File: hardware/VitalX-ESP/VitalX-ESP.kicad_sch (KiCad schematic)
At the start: 45 parts, among them J1 ECG Probe, J2 GSR Probe, Q1 BSS138, U1 AD8232ACPZ-R7, U2 ESP32-WROOM-32U, U3 ADP160AUJZ-1.8-R7, U4 ADPD144RI-ACEZ-RL, U5 AMS1117-3.3, U6 MCP601-xOT

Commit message: [nightly] Initial esp32-s2-wroom configuration.
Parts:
- removed U2: ESP32-WROOM-32U, RF_Module:ESP32-WROOM-32U, symbol RF_Module:ESP32-WROOM-32U
- added C14: 22u, Capacitor_SMD:C_0603_1608Metric, symbol Device:C_Small
- added C15: 100n, Capacitor_SMD:C_0603_1608Metric, symbol Device:C_Small
- added C16: 1u, Capacitor_SMD:C_0603_1608Metric, symbol Device:C_Small
- added J3: UART, symbol Connector_Generic:Conn_01x04
- added R24, R25: 10K, Resistor_SMD:R_0603_1608Metric, symbol Device:R
- added U7: ESP32-S2-WROOM, symbol ESP32-S2-WROOM:esp32-s2-wroom
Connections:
- net +3V3: now also C14.1, C15.1, J3.1 (Pin_1), R24.1, R25.2, U7.2 (3.3v)
- net GND: now also C14.2, C15.2, C16.1, J3.4 (Pin_4), U7.1 (GND), U7.26 (GND), U7.42 (GND), U7.43 (GND)
- new net: J3.3 (Pin_3), U7.37 (TXD0)
- new net: J3.2 (Pin_2), U7.38 (RXD0)
- new net: C16.2, R24.2, U7.41 (EN)
- new net U1RXD: R25.1, U7.21 (IO18)
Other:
- note added: "note: LOD (lead of detection) +- & SDN are digital pin"
- note added: "these are analog"
- moved on the sheet: C1, C10, C11, C12, C13, C2, C3, C4, C5, C6, C7, C8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

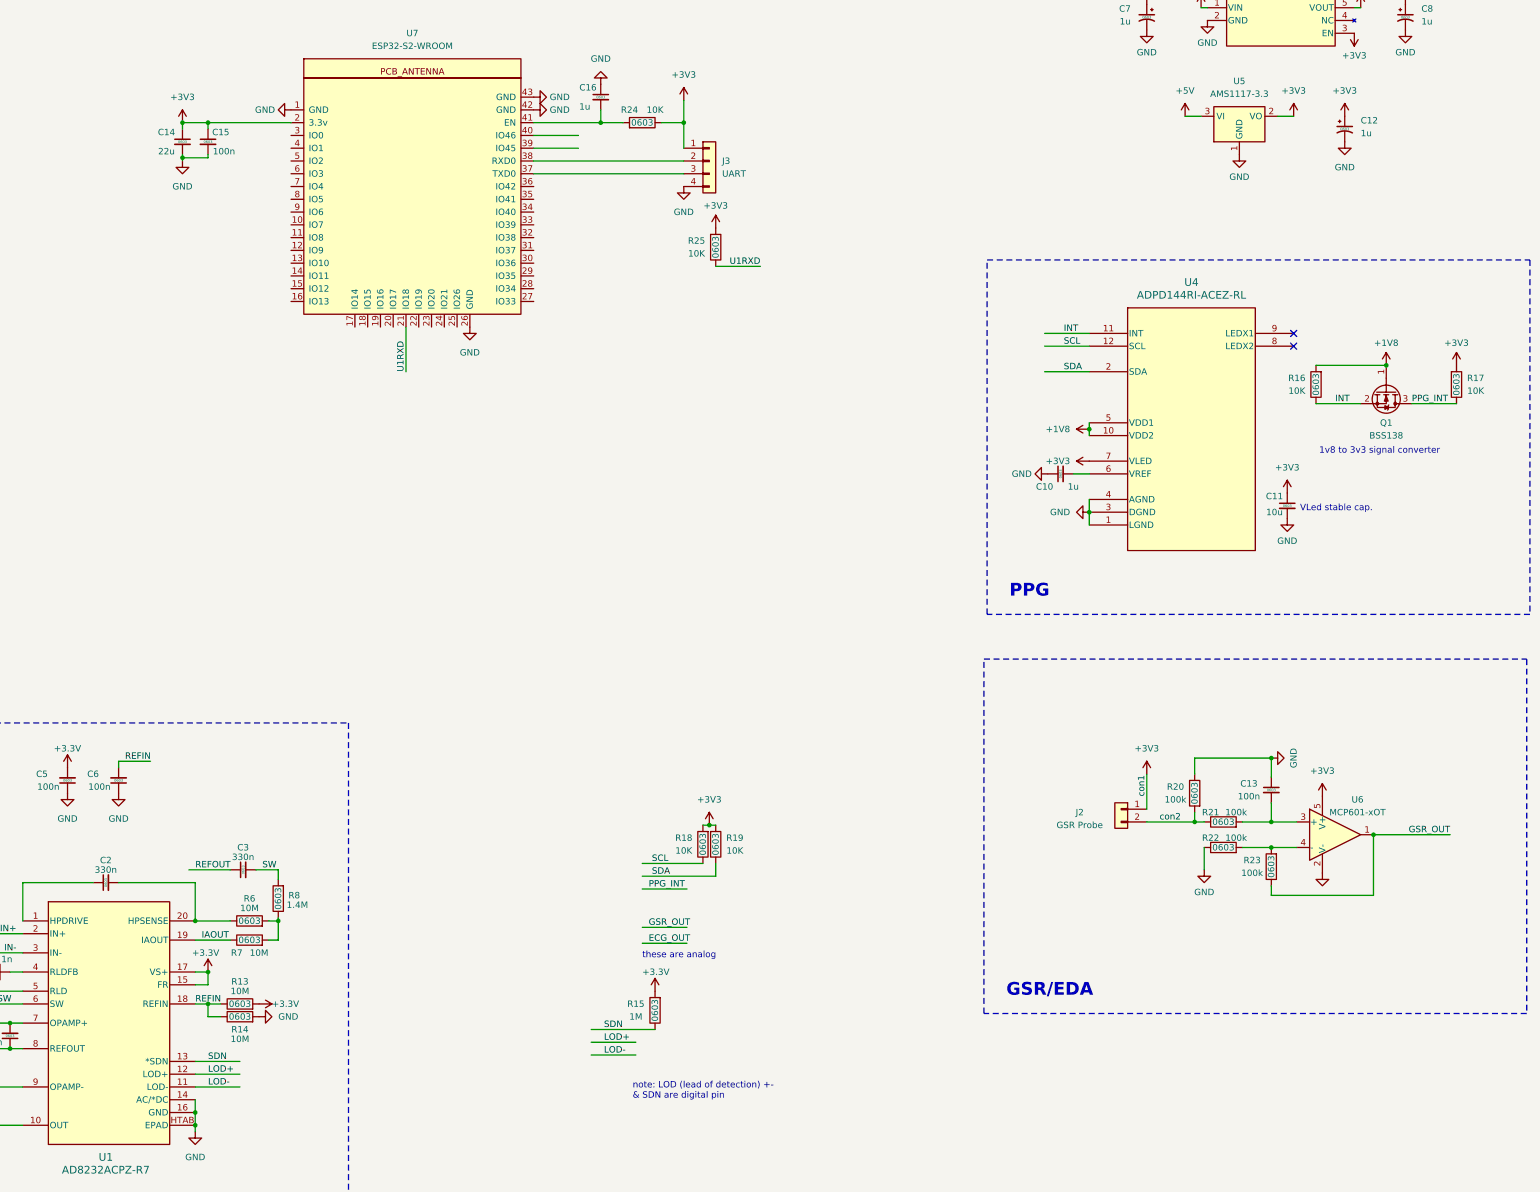
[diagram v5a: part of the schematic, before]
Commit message: [nightly] Connect peripherals.
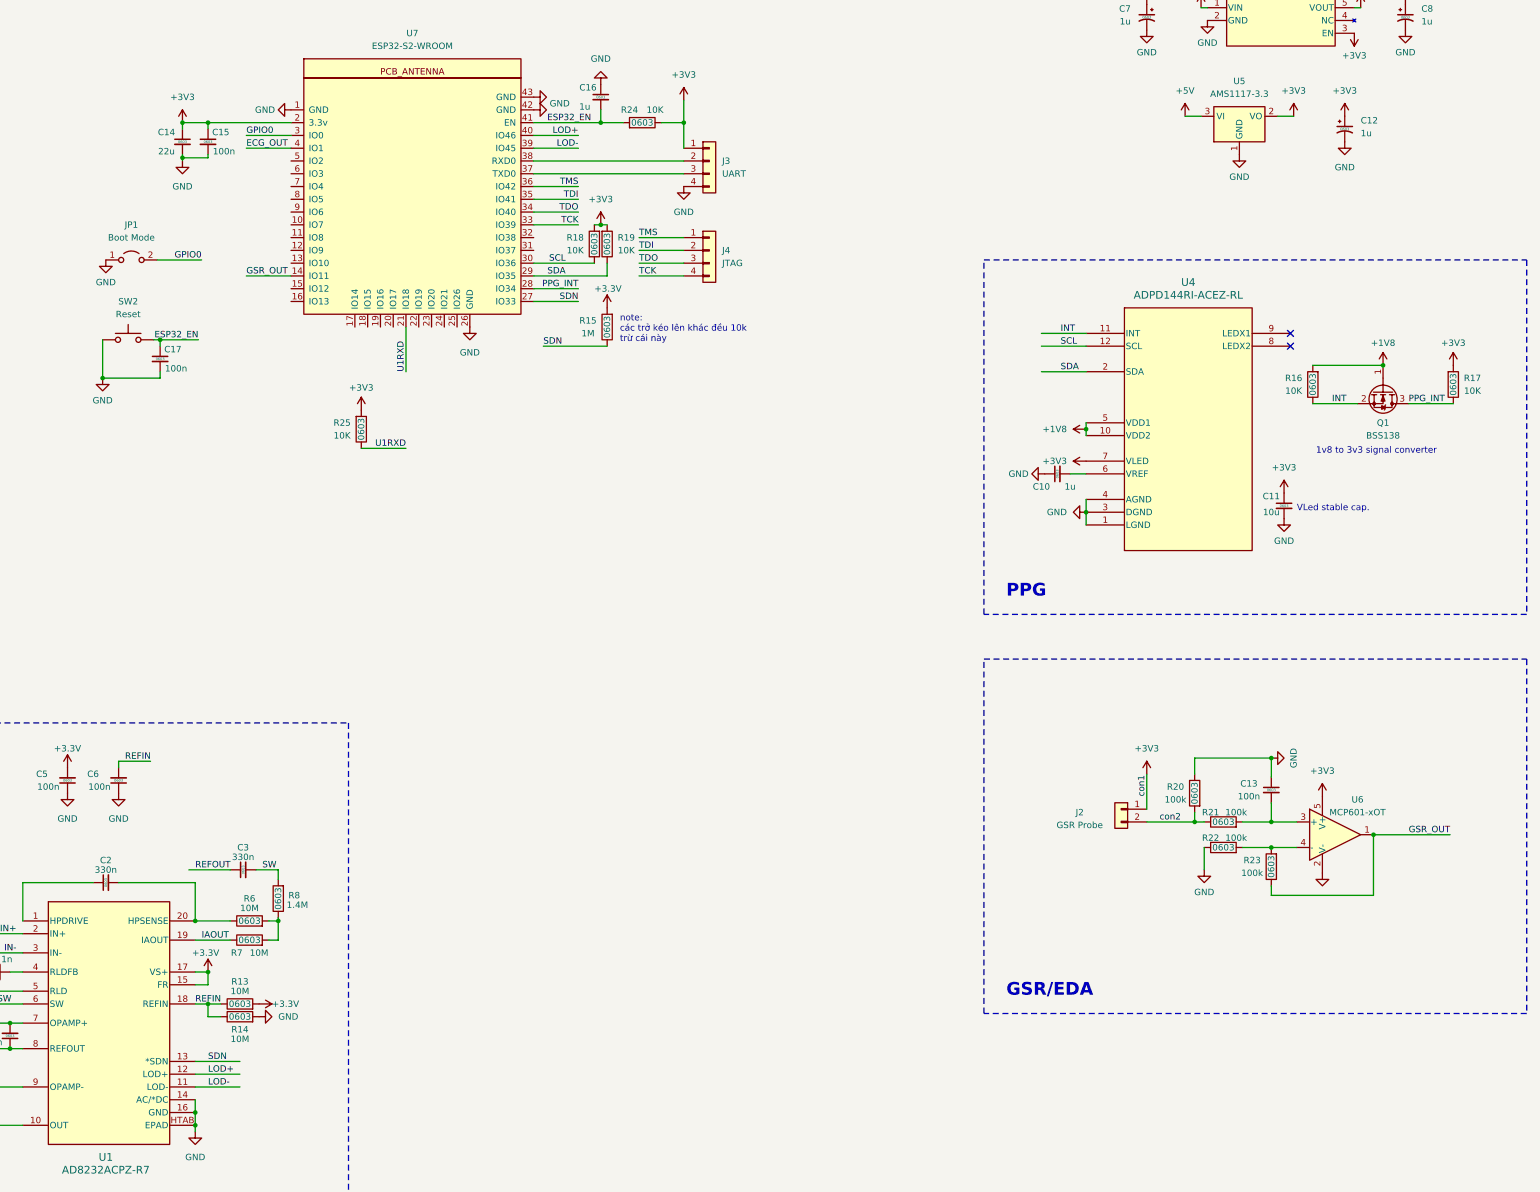
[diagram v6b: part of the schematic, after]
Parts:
- added C17: 100n, Capacitor_SMD:C_0603_1608Metric, symbol Device:C_Small
- added J4: JTAG, symbol Connector_Generic:Conn_01x04
- added JP1: Boot Mode, symbol Jumper:Jumper_2_Open
- added SW2: Reset, symbol Switch:SW_Push
- U7: footprint (none) -> ESP32-S2-WROOM:esp32-s2-wrooom
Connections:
- net ECG_OUT: now also U7.4 (IO1)
- net GND: now also C17.2, JP1.1 (A), SW2.1
- net GSR_OUT: now also U7.14 (IO11)
- net LOD+: now also U7.40 (IO46)
- net LOD-: now also U7.39 (IO45)
- net PPG_INT: now also U7.28 (IO34)
- net SCL: now also U7.30 (IO36)
- net SDA: now also U7.29 (IO35)
- net SDN: now also U7.27 (IO33)
- net GPIO0: now reaches U7.3 (IO0)
- net GPIO0: now also JP1.2 (B)
- net TCK: now reaches U7.33 (IO39)
- net TCK: now also J4.4 (Pin_4)
- net TDO: now reaches U7.34 (IO40)
- net TDO: now also J4.3 (Pin_3)
- net TDI: now reaches U7.35 (IO41)
- net TDI: now also J4.2 (Pin_2)
- net TMS: now reaches U7.36 (IO42)
- net TMS: now also J4.1 (Pin_1)
- net ESP32_EN: now reaches C16.2, R24.2, U7.41 (EN)
- net ESP32_EN: now also C17.1, SW2.2
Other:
- note added: "note: các trở kéo lên khác đều 10k trừ cái này"
- note removed: "note: LOD (lead of detection) +- & SDN are digital pin"
- note removed: "these are analog"
- moved on the sheet: C10, C11, Q1, R15, R16, R17, R18, R19, R25, U4

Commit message: [nightly] Finalize schematic, ERC exclutions.
Exclude typical power-in power-out ERC errors.
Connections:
- net con2: no longer names the net of J2.2 (Pin_2), R20.2, R21.1
- no-connect marks 2 -> 23
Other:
- note added: "MCU"
- note added: "POWER"
- note added: "note: all pull-up resistors are 10k except this one."
- note removed: "note: các trở kéo lên khác đều 10k trừ cái này"
- moved on the sheet: C1, C10, C11, C12, C13, C14, C15, C16, C17, C2, C3, C4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

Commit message: [nightly] Asign footprint.
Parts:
- J1: footprint Connector_Audio:Jack_3.5mm_CUI_SJ2-3593D-SMT_Horizontal -> AUDIO_SJ2-3574A-SMT-TR:SJ2-3574A-SMT-TR
- J3, J4: footprint (none) -> Connector_PinHeader_2.54mm:PinHeader_1x04_P2.54mm_Vertical_SMD_Pin1Left
- JP1: footprint (none) -> Connector_PinHeader_2.54mm:PinHeader_1x02_P2.54mm_Vertical_SMD_Pin1Left
- SW2: footprint (none) -> Button_Switch_THT:SW_PUSH_1P1T_6x3.5mm_H5.0_APEM_MJTP1250
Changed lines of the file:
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@@
       (effects (font (size 1.27 1.27)))
     )
-    (property "Footprint" "" (at 88.9 104.775 0)
+    (property "Footprint" "Button_Switch_THT:SW_PUSH_1P1T_6x3.5mm_H5.0_APEM_MJTP1250" (at 88.9 104.775 0)
       (effects (font (size 1.27 1.27)) hide)
     )
@@
       (effects (font (size 1.27 1.27)))
     )
-    (property "Footprint" "Connector_Audio:Jack_3.5mm_CUI_SJ2-3593D-SMT_Horizontal" (at 40.005 198.755 0)
+    (property "Footprint" "AUDIO_SJ2-3574A-SMT-TR:SJ2-3574A-SMT-TR" (at 40.005 198.755 0)
       (effects (font (size 1.27 1.27)) hide)
     )
@@
       (effects (font (size 1.27 1.27)))
     )
-    (property "Footprint" "" (at 89.535 93.98 0)
+    (property "Footprint" "Connector_PinHeader_2.54mm:PinHeader_1x02_P2.54mm_Vertical_SMD_Pin1Left" (at 89.535 93.98 0)
       (effects (font (size 1.27 1.27)) hide)
     )
@@
       (effects (font (size 1.27 1.27)) (justify left))
     )
-    (property "Footprint" "" (at 204.47 92.075 0)
+    (property "Footprint" "Connector_PinHeader_2.54mm:PinHeader_1x04_P2.54mm_Vertical_SMD_Pin1Left" (at 204.47 92.075 0)
       (effects (font (size 1.27 1.27)) hide)
     )
@@
       (effects (font (size 1.27 1.27)) (justify left))
     )
-    (property "Footprint" "" (at 204.47 74.295 0)
-      (effects (font (size 1.27 1.27)) hide)
-    )
+    (property "Footprint" "Connector_PinHeader_2.54mm:PinHeader_1x04_P2.54mm_Vertical_SMD_Pin1Left" (at 204.47 74.295 0)
+      (effects (font (size 1.27 1.27)) hide)
+    )
